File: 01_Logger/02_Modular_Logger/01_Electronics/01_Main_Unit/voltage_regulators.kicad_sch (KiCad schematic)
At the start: 22 parts, among them Q601 BSS123, Q602 IRLML6401, Q603 BSS123, Q604 IRLML6401, U601 SPBW06F-12, U602 OKI-78SR-3.3_1.5-W36-C, U603 OKI-78SR-5_1.5-W36-C

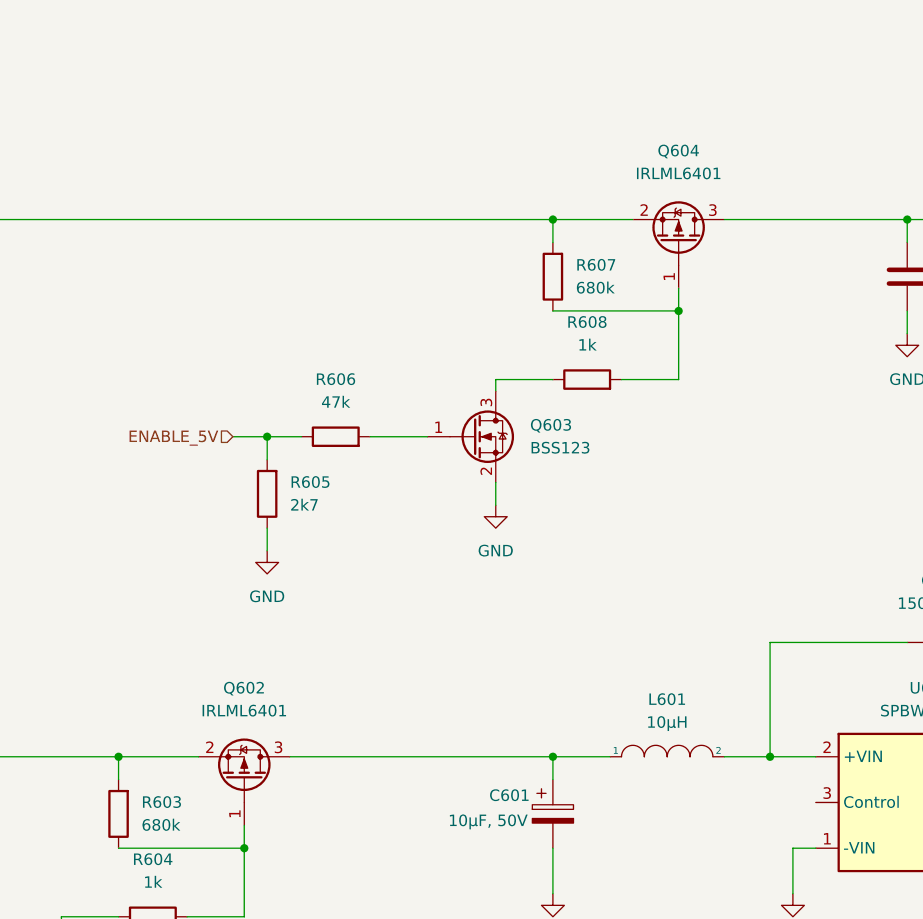
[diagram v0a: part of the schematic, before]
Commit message: update Electronics for Modular_Logger
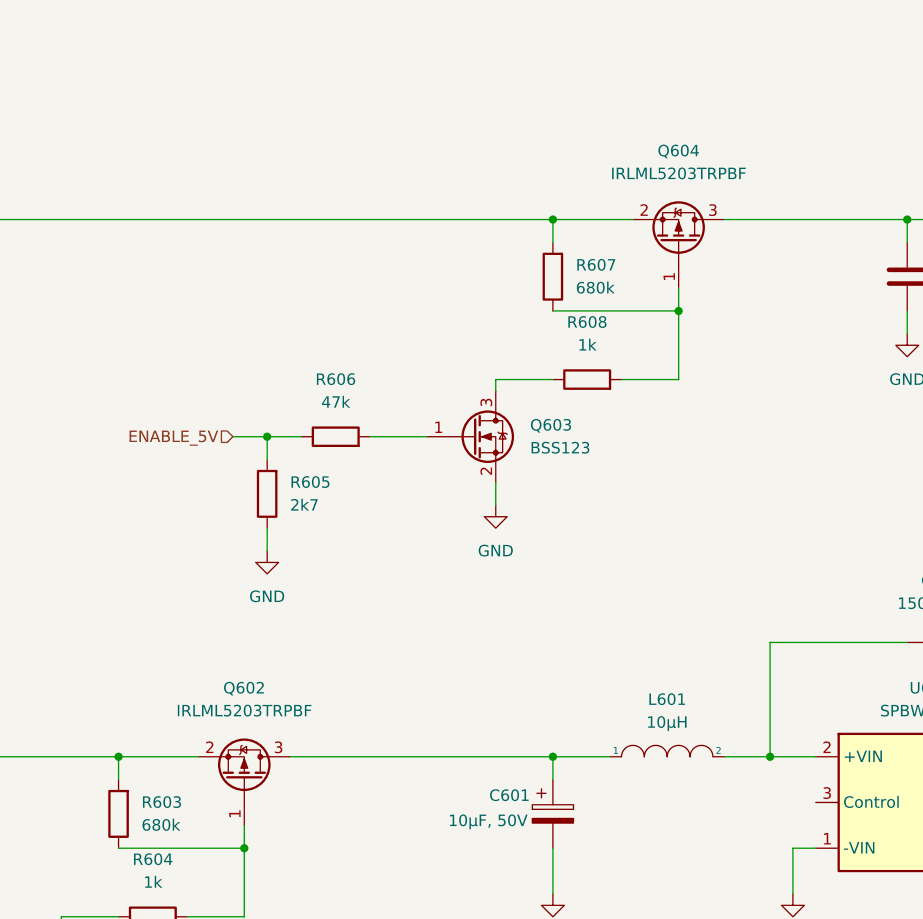
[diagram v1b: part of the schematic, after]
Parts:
- Q602, Q604: value IRLML6401 -> IRLML5203TRPBF
